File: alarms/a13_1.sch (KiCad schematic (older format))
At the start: 41 parts, among them U13001 74HC04, U13002 74HC02, U13003 74HC02, U13004 74HC27, U13005 74HC02, U13006 74LVC07, U13007 74HC27, U13008 74HC02, U13009 74HC4002, U13010 74HC02, U13011 74HC4002, U13012 74HC02, U13013 74HC27, U13014 74HC02, U13015 74HC02, U13016 74HC04, U13017 74HC27, U13018 74HC02, U13019 74HC27, U13020 74HC02, U13021 74LVC07, U13022 74HC02, U13023 74HC04, U13024 74HC02, U13025 74HC02, U13026 74HC27, U13027 74HC04, U13028 74HC4002, U13029 74HC02, U13030 74HC27, U13031 74HC02, U13032 74HC04, U13033 74HC4002, U13034 74HC4002, U13035 74HC4002, U13036 74LVC07, U13047 74HC04, U13049 74HC02

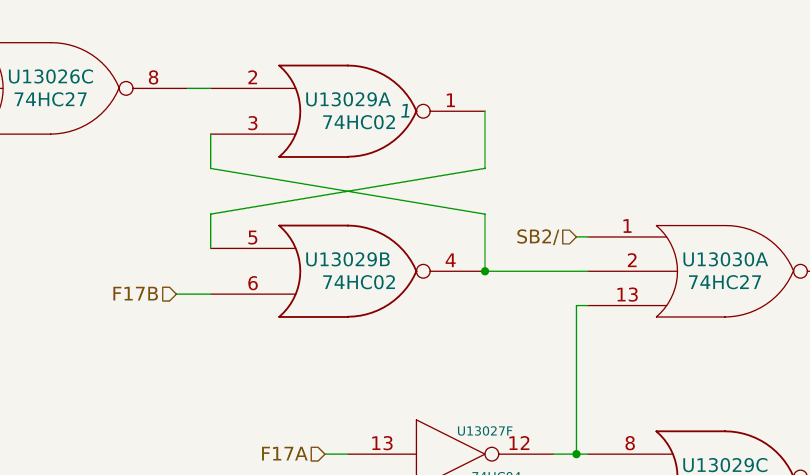
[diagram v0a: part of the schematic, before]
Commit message: Corrected a wiring error in the Monitor request logic (ST1 in place of ST0) and an initial condition problem in the scaler causing the computer to come up with night watchman alarm
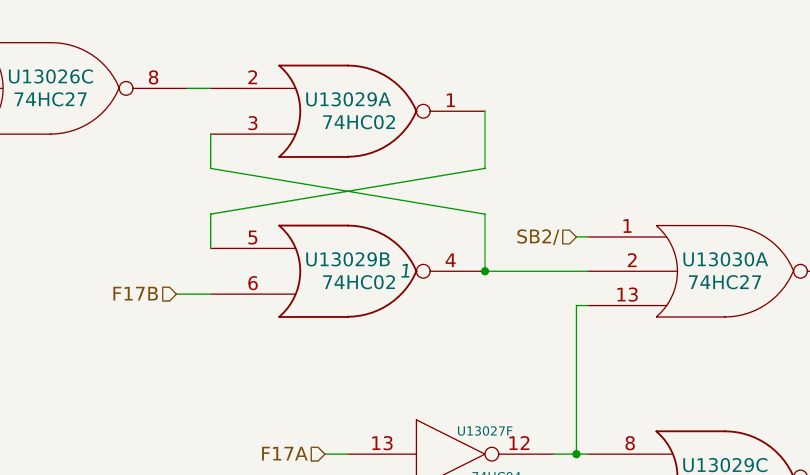
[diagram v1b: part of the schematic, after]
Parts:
- U13029: Initial 1 -> (none)
- U13029: Initial (none) -> 1
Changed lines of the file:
@@
 F 2 "" H 16000 1150 60  0000 C CNN
 F 3 "" H 16000 1150 60  0000 C CNN
-F 4 "1" H 16250 1150 60  0000 C CIN "Initial"
 	1    16000 1150
 	1    0    0    -1
@@
 F 2 "" H 16000 1850 60  0000 C CNN
 F 3 "" H 16000 1850 60  0000 C CNN
+F 4 "1" H 16250 1850 60  0000 C CIN "Initial"
 	2    16000 1850
 	1    0    0    -1

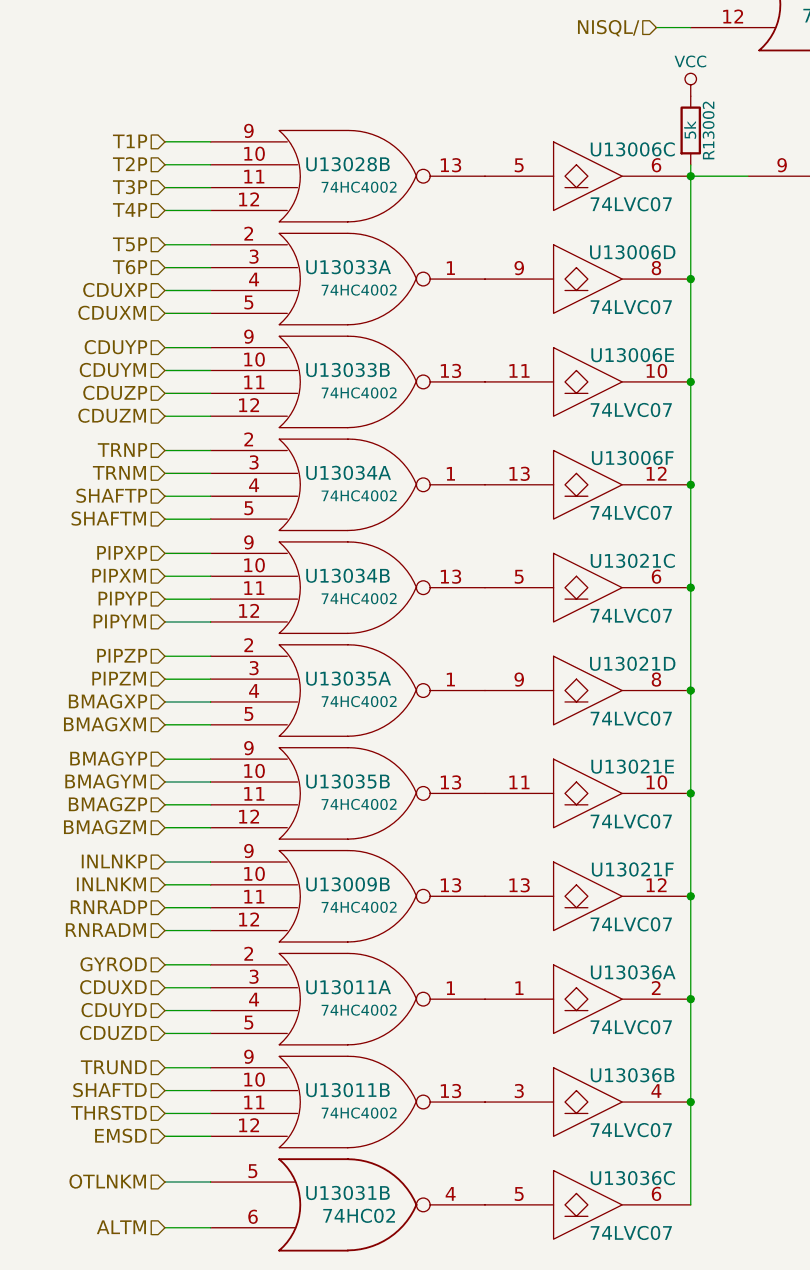
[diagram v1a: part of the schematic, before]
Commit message: Some initial condition updates to fix a couple oscillating signals I found
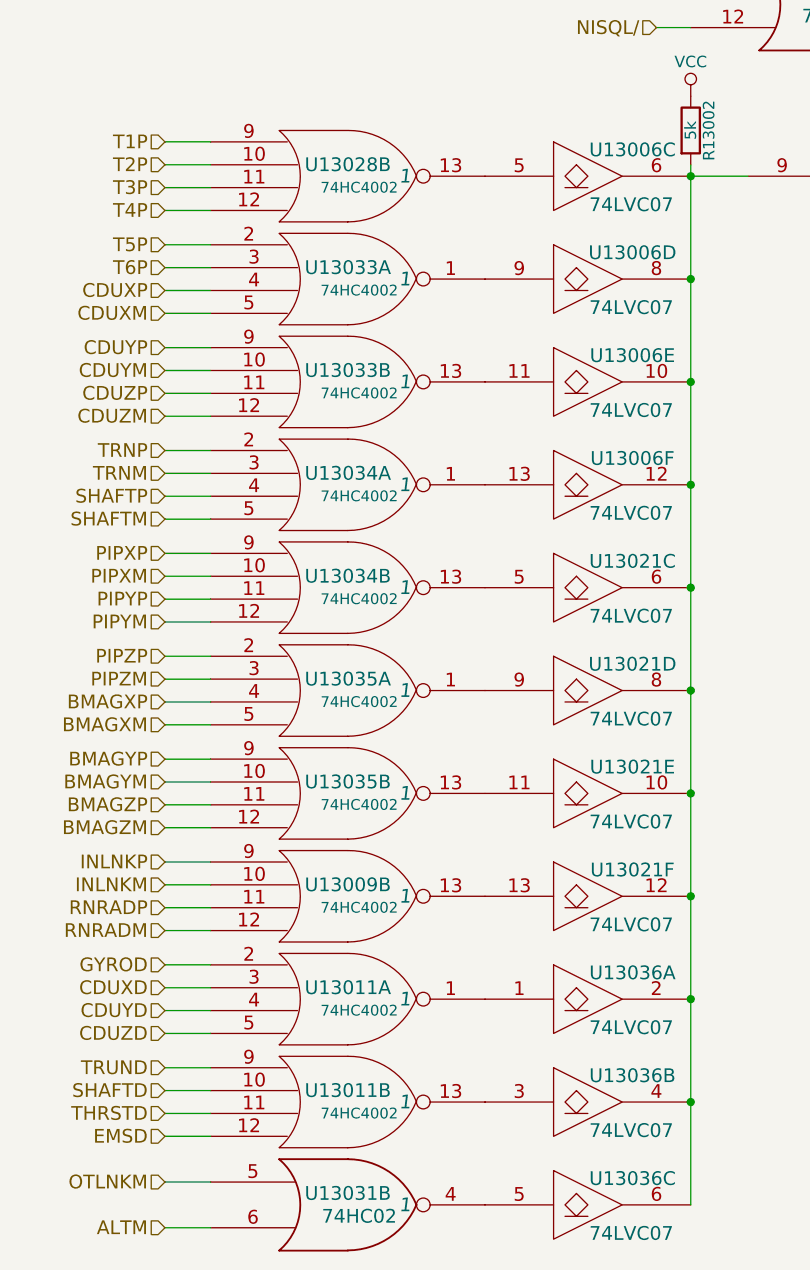
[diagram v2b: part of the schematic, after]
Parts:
- U13009, U13011, U13028, U13031, U13033, U13034, U13035: Initial (none) -> 1
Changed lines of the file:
@@
 F 2 "" H 11100 13750 60  0000 C CNN
 F 3 "" H 11100 13750 60  0000 C CNN
+F 4 "1" H 11350 13750 60  0000 C CIN "Initial"
 	2    11100 13750
 	1    0    0    -1
@@
 F 2 "" H 11100 14200 60  0000 C CNN
 F 3 "" H 11100 14200 60  0000 C CNN
+F 4 "1" H 11350 14200 60  0000 C CIN "Initial"
 	1    11100 14200
 	1    0    0    -1
@@
 F 2 "" H 11100 14650 60  0000 C CNN
 F 3 "" H 11100 14650 60  0000 C CNN
+F 4 "1" H 11350 14650 60  0000 C CIN "Initial"
 	2    11100 14650
 	1    0    0    -1
@@
 F 2 "" H 11100 10600 60  0000 C CNN
 F 3 "" H 11100 10600 60  0000 C CNN
+F 4 "1" H 11350 10600 60  0000 C CIN "Initial"
 	2    11100 10600
 	1    0    0    -1
@@
 F 2 "" H 11100 11050 60  0000 C CNN
 F 3 "" H 11100 11050 60  0000 C CNN
+F 4 "1" H 11350 11050 60  0000 C CIN "Initial"
 	1    11100 11050
 	1    0    0    -1
@@
 F 2 "" H 11100 11500 60  0000 C CNN
 F 3 "" H 11100 11500 60  0000 C CNN
+F 4 "1" H 11350 11500 60  0000 C CIN "Initial"
 	2    11100 11500
 	1    0    0    -1
@@
 F 2 "" H 11100 11950 60  0000 C CNN
 F 3 "" H 11100 11950 60  0000 C CNN
+F 4 "1" H 11350 11950 60  0000 C CIN "Initial"
 	1    11100 11950
 	1    0    0    -1
@@
 F 2 "" H 11100 12400 60  0000 C CNN
 F 3 "" H 11100 12400 60  0000 C CNN
+F 4 "1" H 11350 12400 60  0000 C CIN "Initial"
 	2    11100 12400
 	1    0    0    -1
@@
 F 2 "" H 11100 12850 60  0000 C CNN
 F 3 "" H 11100 12850 60  0000 C CNN
+F 4 "1" H 11350 12850 60  0000 C CIN "Initial"
 	1    11100 12850
 	1    0    0    -1
@@
 F 2 "" H 11100 13300 60  0000 C CNN
 F 3 "" H 11100 13300 60  0000 C CNN
+F 4 "1" H 11350 13300 60  0000 C CIN "Initial"
 	2    11100 13300
 	1    0    0    -1
@@
 F 2 "" H 11100 15100 60  0000 C CNN
 F 3 "" H 11100 15100 60  0000 C CNN
+F 4 "1" H 11350 15100 60  0000 C CIN "Initial"
 	2    11100 15100
 	1    0    0    -1

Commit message: Fixed not->1-input nor in the rest of the modules.
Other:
- moved on the sheet: R13001, R13002, R13003, U13001A, U13001B, U13001C, U13001D, U13001E, U13001F, U13002A, U13002B, U13002C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

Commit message: Set up Alarms for +4VDC and +4VSW power nets. Pretty sure I got all the standby stuff...
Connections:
- net labels added: +4VDC, +4VSW
- net labels removed: VCC
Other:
- moved on the sheet: U13116D, U13118D, U13123E

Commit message: Added the CH77 alarm box (restart monitor) and switched most (all?) monitor outputs over to open drain, largely using new 74LVC06 parts (which are used *only* for monitor outputs)
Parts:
- removed unit 2 of U13016
- removed unit 4 of U13016
- removed unit 4 of U13023
- removed unit 3 of U13023
- removed unit 5 of U13023
- removed U13027, U13032: 74HC04, symbol 74HC04
- added U13051: 74LVC07, symbol 74LVC07
- added U13052, U13053: 74LVC06, symbol 74LVC06
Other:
- moved on the sheet: R13001, U13004B, U13004C, U13006A, U13006B, U13014D, U13126B, U13127C, U13127D, U13128A

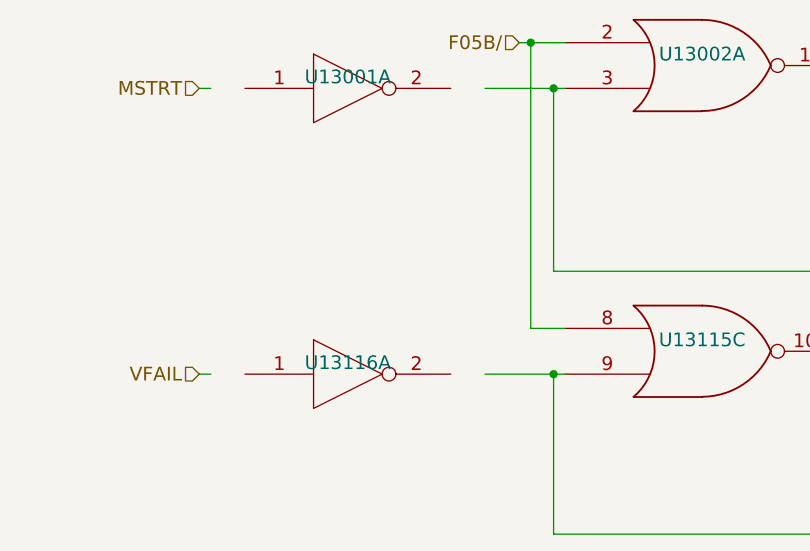
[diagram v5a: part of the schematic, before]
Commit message: Some initial condition updates for the CH77 alarm box and a monitor output I missed converting to 74LVC06
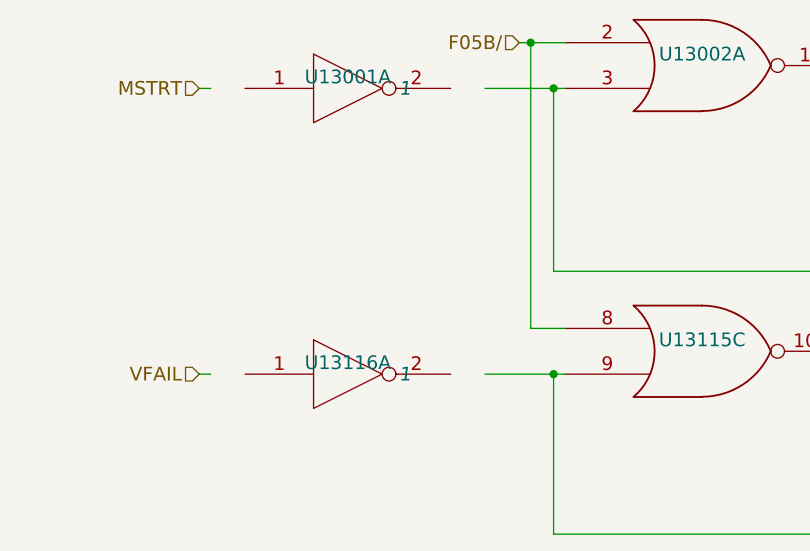
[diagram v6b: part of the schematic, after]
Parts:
- U13001, U13016: Initial (none) -> 1
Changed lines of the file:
@@
 LIBS:valves
 LIBS:agc_kicad_components
-EELAYER 25 0
+EELAYER 26 0
 EELAYER END
 $Descr A2 23386 16535
@@
 F 2 "" H 3400 1000 60  0000 C CNN
 F 3 "" H 3400 1000 60  0000 C CNN
+F 4 "1" H 3650 1000 60  0000 C CIN "Initial"
 	1    3400 1000
 	1    0    0    -1
@@
 F 2 "" H 3400 2250 60  0000 C CNN
 F 3 "" H 3400 2250 60  0000 C CNN
+F 4 "1" H 3650 2250 60  0000 C CIN "Initial"
 	1    3400 2250
 	1    0    0    -1
